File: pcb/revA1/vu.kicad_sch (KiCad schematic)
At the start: 32 parts

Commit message: revA1, WIP
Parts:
- renumbered R30 to R33, R31 to R34, R32 to R35, R33 to R36, R34 to R37, R35 to R38, R36 to R39, R37 to R40, R38 to R41, R39 to R42, R40 to R43, R41 to R44, R42 to R45, R43 to R46, R44 to R47, R45 to R48
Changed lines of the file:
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@@
 		(in_pos_files yes)
 		(dnp no)
-		(property "Reference" "R31"
+		(property "Reference" "R34"
 			(at 59.69 43.815 90)
 			(show_name no)
@@
 			(project "karabas-megabuzz"
 				(path "/eff1afb7-47ba-46af-a815-4a07fb8d674b/13ede702-d735-4dea-a3c9-12f9e8dd6d62"
-					(reference "R31")
+					(reference "R34")
 					(unit 1)
 				)
@@
 		(in_pos_files yes)
 		(dnp no)
-		(property "Reference" "R40"
+		(property "Reference" "R43"
 			(at 81.28 51.435 90)
 			(show_name no)
@@
 			(project "karabas-megabuzz"
 				(path "/eff1afb7-47ba-46af-a815-4a07fb8d674b/13ede702-d735-4dea-a3c9-12f9e8dd6d62"
-					(reference "R40")
+					(reference "R43")
 					(unit 1)
 				)
@@
 		(in_pos_files yes)
 		(dnp no)
-		(property "Reference" "R38"
+		(property "Reference" "R41"
 			(at 81.28 36.195 90)
 			(show_name no)
@@
 			(project "karabas-megabuzz"
 				(path "/eff1afb7-47ba-46af-a815-4a07fb8d674b/13ede702-d735-4dea-a3c9-12f9e8dd6d62"
-					(reference "R38")
+					(reference "R41")
 					(unit 1)
 				)
@@
 		(in_pos_files yes)
 		(dnp no)
-		(property "Reference" "R34"
+		(property "Reference" "R37"
 			(at 59.69 66.675 90)
 			(show_name no)
@@
 			(project "karabas-megabuzz"
 				(path "/eff1afb7-47ba-46af-a815-4a07fb8d674b/13ede702-d735-4dea-a3c9-12f9e8dd6d62"
-					(reference "R34")
+					(reference "R37")
 					(unit 1)
 				)
@@
 		(in_pos_files yes)
 		(dnp no)
-		(property "Reference" "R45"
+		(property "Reference" "R48"
 			(at 81.28 89.535 90)
 			(show_name no)
@@
 			(project "karabas-megabuzz"
 				(path "/eff1afb7-47ba-46af-a815-4a07fb8d674b/13ede702-d735-4dea-a3c9-12f9e8dd6d62"
-					(reference "R45")
+					(reference "R48")
 					(unit 1)
 				)
@@
 		(in_pos_files yes)
 		(dnp no)
-		(property "Reference" "#PWR0131"
+		(property "Reference" "#PWR0143"
 			(at 68.58 38.1 0)
 			(hide yes)
@@
 			(project "karabas-megabuzz"
 				(path "/eff1afb7-47ba-46af-a815-4a07fb8d674b/13ede702-d735-4dea-a3c9-12f9e8dd6d62"
-					(reference "#PWR0131")
+					(reference "#PWR0143")
 					(unit 1)
 				)
@@
 		(in_pos_files yes)
 		(dnp no)
-		(property "Reference" "R36"
+		(property "Reference" "R39"
 			(at 59.69 81.915 90)
 			(show_name no)
@@
 			(project "karabas-megabuzz"
 				(path "/eff1afb7-47ba-46af-a815-4a07fb8d674b/13ede702-d735-4dea-a3c9-12f9e8dd6d62"
-					(reference "R36")
+					(reference "R39")
 					(unit 1)
 				)
@@
 		(in_pos_files yes)
 		(dnp no)
-		(property "Reference" "R44"
+		(property "Reference" "R47"
 			(at 81.28 81.915 90)
 			(show_name no)
@@
 			(project "karabas-megabuzz"
 				(path "/eff1afb7-47ba-46af-a815-4a07fb8d674b/13ede702-d735-4dea-a3c9-12f9e8dd6d62"
-					(reference "R44")
+					(reference "R47")
 					(unit 1)
 				)
@@
 		(in_pos_files yes)
 		(dnp no)
-		(property "Reference" "#PWR0136"
+		(property "Reference" "#PWR0144"
 			(at 72.39 38.1 0)
 			(hide yes)
@@
 			(project "karabas-megabuzz"
 				(path "/eff1afb7-47ba-46af-a815-4a07fb8d674b/13ede702-d735-4dea-a3c9-12f9e8dd6d62"
-					(reference "#PWR0136")
+					(reference "#PWR0144")
 					(unit 1)
 				)
@@
 		(in_pos_files yes)
 		(dnp no)
-		(property "Reference" "R37"
+		(property "Reference" "R40"
 			(at 59.69 89.535 90)
 			(show_name no)
@@
 			(project "karabas-megabuzz"
 				(path "/eff1afb7-47ba-46af-a815-4a07fb8d674b/13ede702-d735-4dea-a3c9-12f9e8dd6d62"
-					(reference "R37")
+					(reference "R40")
 					(unit 1)
 				)
@@
 		(in_pos_files yes)
 		(dnp no)
-		(property "Reference" "R42"
+		(property "Reference" "R45"
 			(at 81.28 66.675 90)
 			(show_name no)
@@
 			(project "karabas-megabuzz"
 				(path "/eff1afb7-47ba-46af-a815-4a07fb8d674b/13ede702-d735-4dea-a3c9-12f9e8dd6d62"
-					(reference "R42")
+					(reference "R45")
 					(unit 1)
 				)
@@
 		(in_pos_files yes)
 		(dnp no)
-		(property "Reference" "R32"
+		(property "Reference" "R35"
 			(at 59.69 51.435 90)
 			(show_name no)
@@
 			(project "karabas-megabuzz"
 				(path "/eff1afb7-47ba-46af-a815-4a07fb8d674b/13ede702-d735-4dea-a3c9-12f9e8dd6d62"
-					(reference "R32")
+					(reference "R35")
 					(unit 1)
 				)
@@
 		(in_pos_files yes)
 		(dnp no)
-		(property "Reference" "R41"
+		(property "Reference" "R44"
 			(at 81.28 59.055 90)
 			(show_name no)
@@
 			(project "karabas-megabuzz"
 				(path "/eff1afb7-47ba-46af-a815-4a07fb8d674b/13ede702-d735-4dea-a3c9-12f9e8dd6d62"
-					(reference "R41")
+					(reference "R44")
 					(unit 1)
 				)
@@
 		(in_pos_files yes)
 		(dnp no)
-		(property "Reference" "R35"
+		(property "Reference" "R38"
 			(at 59.69 74.295 90)
 			(show_name no)
@@
 			(project "karabas-megabuzz"
 				(path "/eff1afb7-47ba-46af-a815-4a07fb8d674b/13ede702-d735-4dea-a3c9-12f9e8dd6d62"
-					(reference "R35")
+					(reference "R38")
 					(unit 1)
 				)
@@
 		(in_pos_files yes)
 		(dnp no)
-		(property "Reference" "R39"
+		(property "Reference" "R42"
 			(at 81.28 43.815 90)
 			(show_name no)
@@
 			(project "karabas-megabuzz"
 				(path "/eff1afb7-47ba-46af-a815-4a07fb8d674b/13ede702-d735-4dea-a3c9-12f9e8dd6d62"
-					(reference "R39")
+					(reference "R42")
 					(unit 1)
 				)
@@
 		(in_pos_files yes)
 		(dnp no)
-		(property "Reference" "R33"
+		(property "Reference" "R36"
 			(at 59.69 59.055 90)
 			(show_name no)
@@
 			(project "karabas-megabuzz"
 				(path "/eff1afb7-47ba-46af-a815-4a07fb8d674b/13ede702-d735-4dea-a3c9-12f9e8dd6d62"
-					(reference "R33")
+					(reference "R36")
 					(unit 1)
 				)
@@
 		(in_pos_files yes)
 		(dnp no)
-		(property "Reference" "R30"
+		(property "Reference" "R33"
 			(at 59.69 36.195 90)
 			(show_name no)
@@
 			(project "karabas-megabuzz"
 				(path "/eff1afb7-47ba-46af-a815-4a07fb8d674b/13ede702-d735-4dea-a3c9-12f9e8dd6d62"
-					(reference "R30")
+					(reference "R33")
 					(unit 1)
 				)
@@
 		(in_pos_files yes)
 		(dnp no)
-		(property "Reference" "R43"
+		(property "Reference" "R46"
 			(at 81.28 74.295 90)
 			(show_name no)
@@
 			(project "karabas-megabuzz"
 				(path "/eff1afb7-47ba-46af-a815-4a07fb8d674b/13ede702-d735-4dea-a3c9-12f9e8dd6d62"
-					(reference "R43")
-					(unit 1)
-				)
+					(reference "R46")
+					(unit 1)
+				)

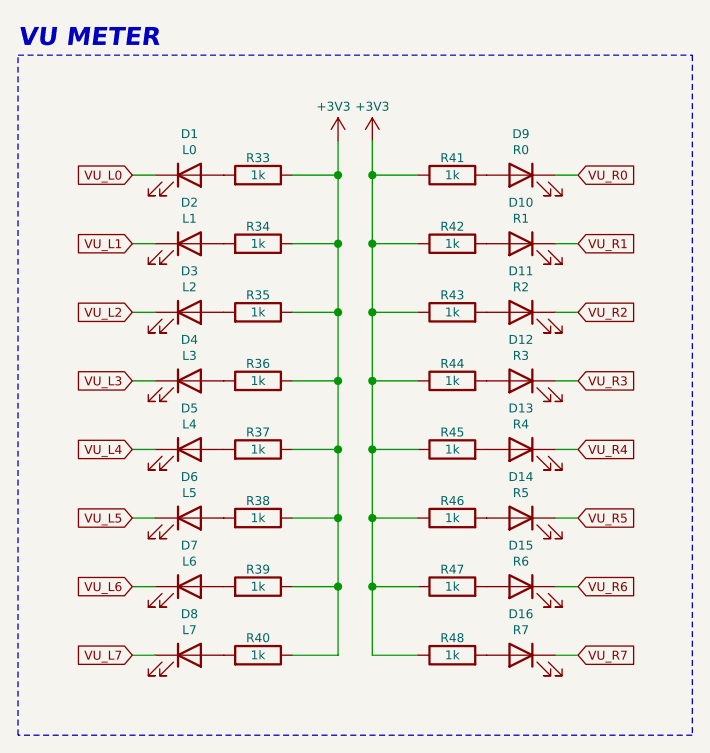
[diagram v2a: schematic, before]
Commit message: Fixed missing LED1 connection, new revA1 release
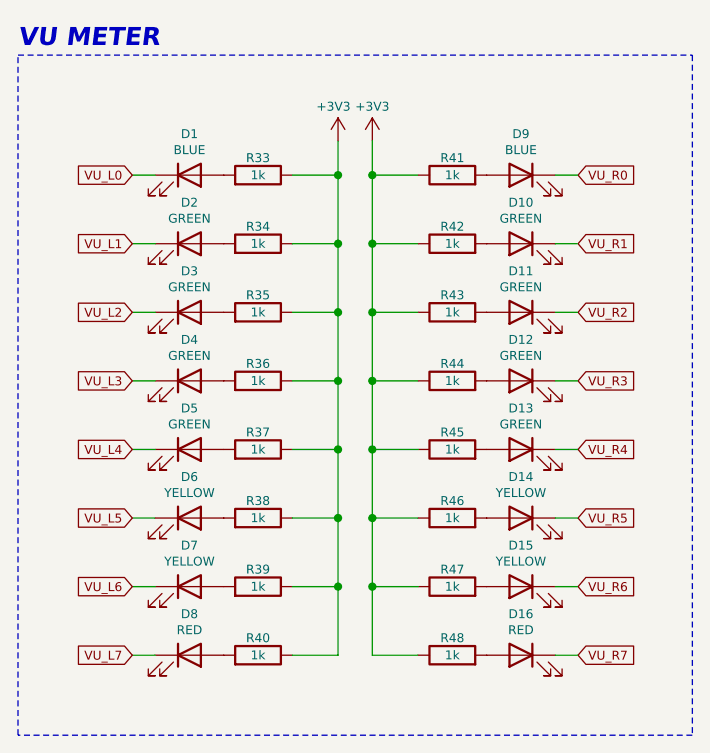
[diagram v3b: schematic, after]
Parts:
- D1: value L0 -> BLUE
- D10: value R1 -> GREEN
- D11: value R2 -> GREEN
- D12: value R3 -> GREEN
- D13: value R4 -> GREEN
- D14: value R5 -> YELLOW
- D15: value R6 -> YELLOW
- D16: value R7 -> RED
- D2: value L1 -> GREEN
- D3: value L2 -> GREEN
- D4: value L3 -> GREEN
- D5: value L4 -> GREEN
- D6: value L5 -> YELLOW
- D7: value L6 -> YELLOW
- D8: value L7 -> RED
- D9: value R0 -> BLUE
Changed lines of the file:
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@@
 			)
 		)
-		(property "Value" "L1"
+		(property "Value" "GREEN"
 			(at 52.07 42.926 0)
 			(show_name no)
@@
 			)
 		)
-		(property "Value" "R6"
+		(property "Value" "YELLOW"
 			(at 88.9 81.026 0)
 			(show_name no)
@@
 			)
 		)
-		(property "Value" "L0"
+		(property "Value" "BLUE"
 			(at 52.07 35.306 0)
 			(show_name no)
@@
 			)
 		)
-		(property "Value" "L6"
+		(property "Value" "YELLOW"
 			(at 52.07 81.026 0)
 			(show_name no)
@@
 			)
 		)
-		(property "Value" "L4"
+		(property "Value" "GREEN"
 			(at 52.07 65.786 0)
 			(show_name no)
@@
 			)
 		)
-		(property "Value" "R3"
+		(property "Value" "GREEN"
 			(at 88.9 58.166 0)
 			(show_name no)
@@
 			)
 		)
-		(property "Value" "L2"
+		(property "Value" "GREEN"
 			(at 52.07 50.546 0)
 			(show_name no)
@@
 			)
 		)
-		(property "Value" "R2"
+		(property "Value" "GREEN"
 			(at 88.9 50.546 0)
 			(show_name no)
@@
 			)
 		)
-		(property "Value" "L7"
+		(property "Value" "RED"
 			(at 52.07 88.646 0)
 			(show_name no)
@@
 			)
 		)
-		(property "Value" "R5"
+		(property "Value" "YELLOW"
 			(at 88.9 73.406 0)
 			(show_name no)
@@
 			)
 		)
-		(property "Value" "R4"
+		(property "Value" "GREEN"
 			(at 88.9 65.786 0)
 			(show_name no)
@@
 			)
 		)
-		(property "Value" "R7"
+		(property "Value" "RED"
 			(at 88.9 88.646 0)
 			(show_name no)
@@
 			)
 		)
-		(property "Value" "R1"
+		(property "Value" "GREEN"
 			(at 88.9 42.926 0)
 			(show_name no)
@@
 			)
 		)
-		(property "Value" "R0"
+		(property "Value" "BLUE"
 			(at 88.9 35.306 0)
 			(show_name no)
@@
 			)
 		)
-		(property "Value" "L5"
+		(property "Value" "YELLOW"
 			(at 52.07 73.406 0)
 			(show_name no)
@@
 			)
 		)
-		(property "Value" "L3"
+		(property "Value" "GREEN"
 			(at 52.07 58.166 0)
 			(show_name no)
